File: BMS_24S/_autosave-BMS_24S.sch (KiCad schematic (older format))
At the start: 30 parts, among them J101 IN, J102 OUT, U101 74HC4051, U102 74HC4051, U103 74HC4051, U104 74HC4051, U105 74HC4051, U106 74HC4051, U107 74HC595, U108 74HC595, U109 74HC595

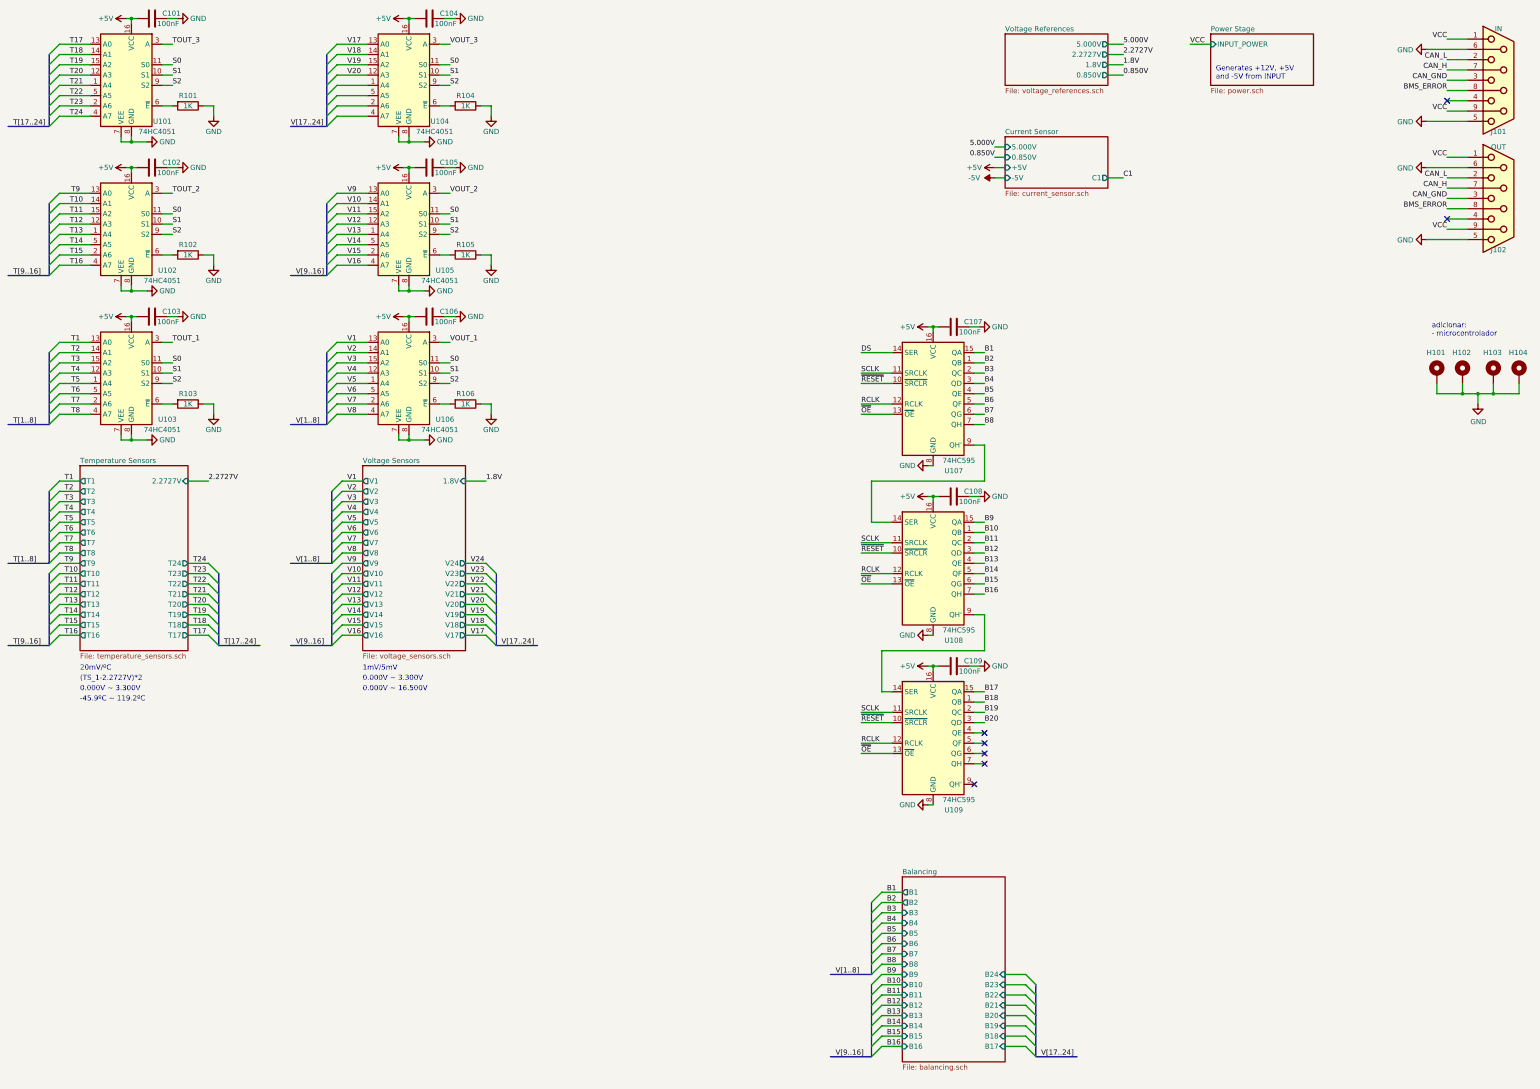
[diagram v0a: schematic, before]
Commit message: correctly positioned voltage sensors and balancing
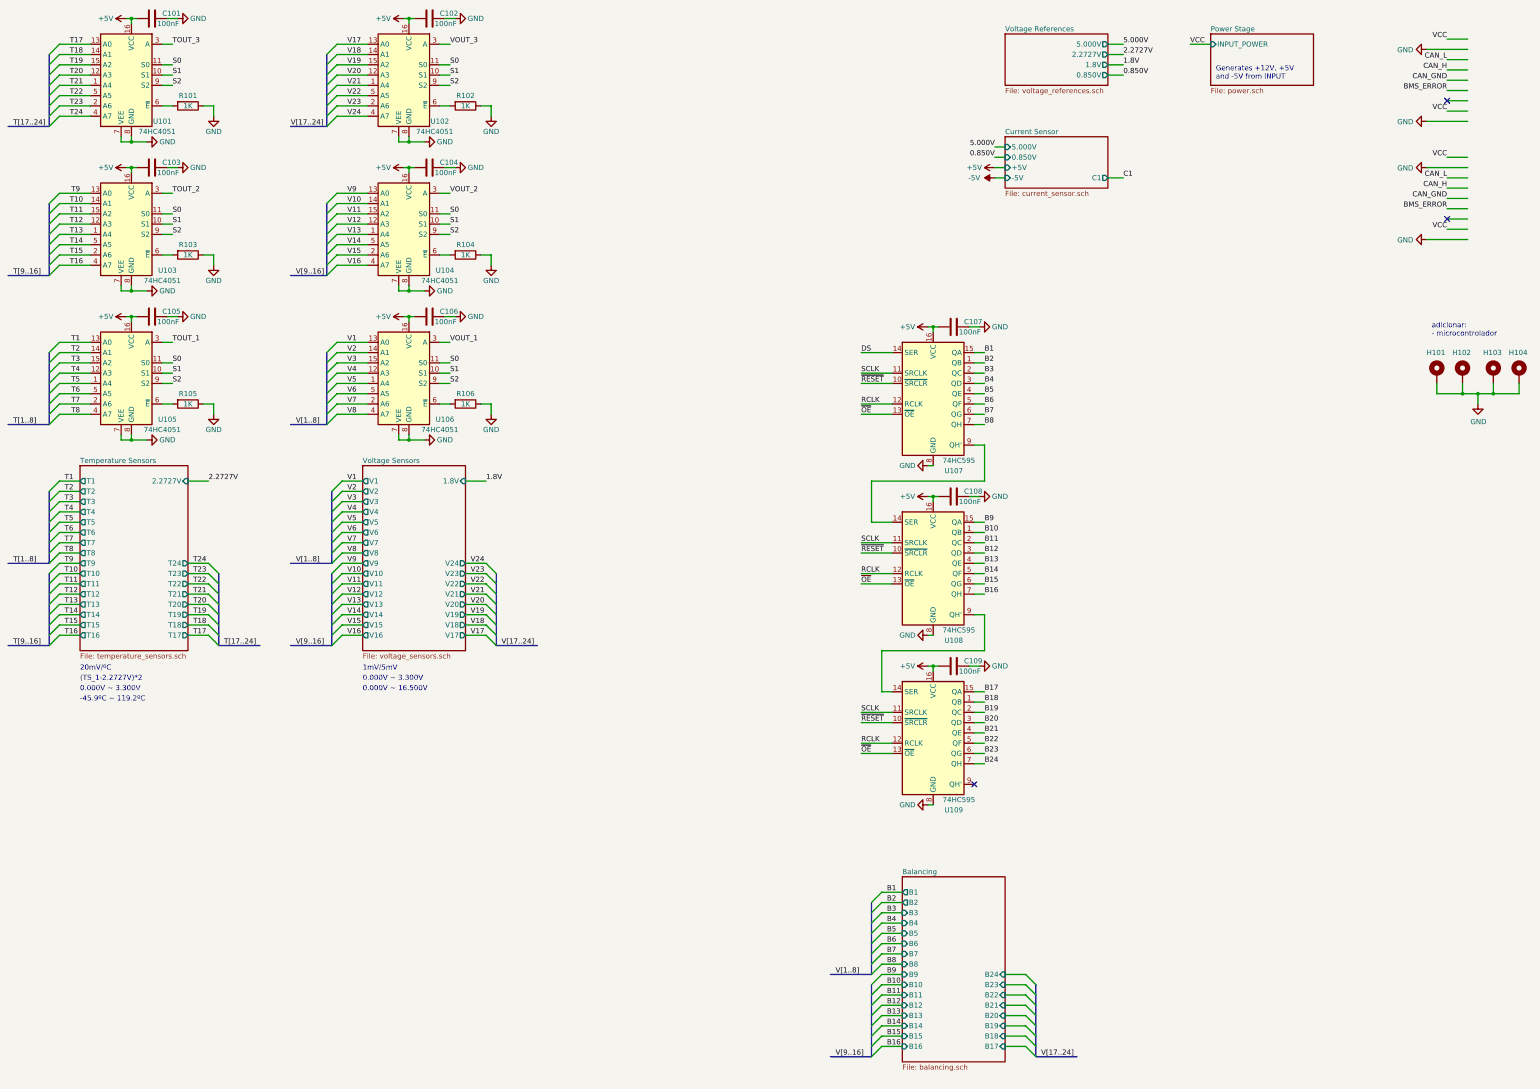
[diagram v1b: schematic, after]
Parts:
- removed J101: IN, e-Power:DSUB-9_Female_EdgeMount_P2.77mm, symbol e-Power:DB9_Female
- removed J102: OUT, e-Power:DSUB-9_Female_EdgeMount_P2.77mm, symbol e-Power:DB9_Female
- renumbered C104 to C102, C102 to C103, C105 to C104, C103 to C105, R104 to R102, R102 to R103, R105 to R104, R103 to R105, U104 to U102, U102 to U103, U105 to U104, U103 to U105
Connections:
- net labels added: B21, B22, B23, B24
- no-connect marks 7 -> 3

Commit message: updated have been made on currents and voltage sensors
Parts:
- added C110, C111: 100nF, Capacitor_SMD:C_0805_2012Metric, symbol Device:C
- added R107, R108, R109, R110, R111, R112, R114, R116, R117, R118, R119, R120, R121, R122, R124, R126, R127, R128, R129, R130, R131, R132, R134, R136: 10K, Resistor_SMD:R_0805_2012Metric, symbol Device:R
- added R113, R115, R123, R125, R133, R135: 1K, Resistor_SMD:R_0805_2012Metric, symbol Device:R
- added U110, U111: LM324, Package_SO:SOIC-14_3.9x8.7mm_P1.27mm, symbol Amplifier_Operational:LM324
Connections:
- net labels added: B[1..8], B[17..24], B[9..16], TOUT_1P, TOUT_2P, TOUT_3P, VOUT_1P, VOUT_2P, VOUT_3P
- wire segments 311 -> 478
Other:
- note added: "(VS_1/5)*3.5\n"
- note added: "0.00V ~~ 2.94V\n"
- note added: "0.00V ~~ 4.20V\n"
- note removed: "0.000V ~~ 16.500V\n"
